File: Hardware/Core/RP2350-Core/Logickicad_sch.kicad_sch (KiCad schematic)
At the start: 31 parts, among them J1 Conn_01x10_Socket, J2 Conn_01x10_Socket, Q1 BSS123, SW1 SW_Push, U17 RP2350A, U19 W25Q16JVSNIQ, X1 12MHz

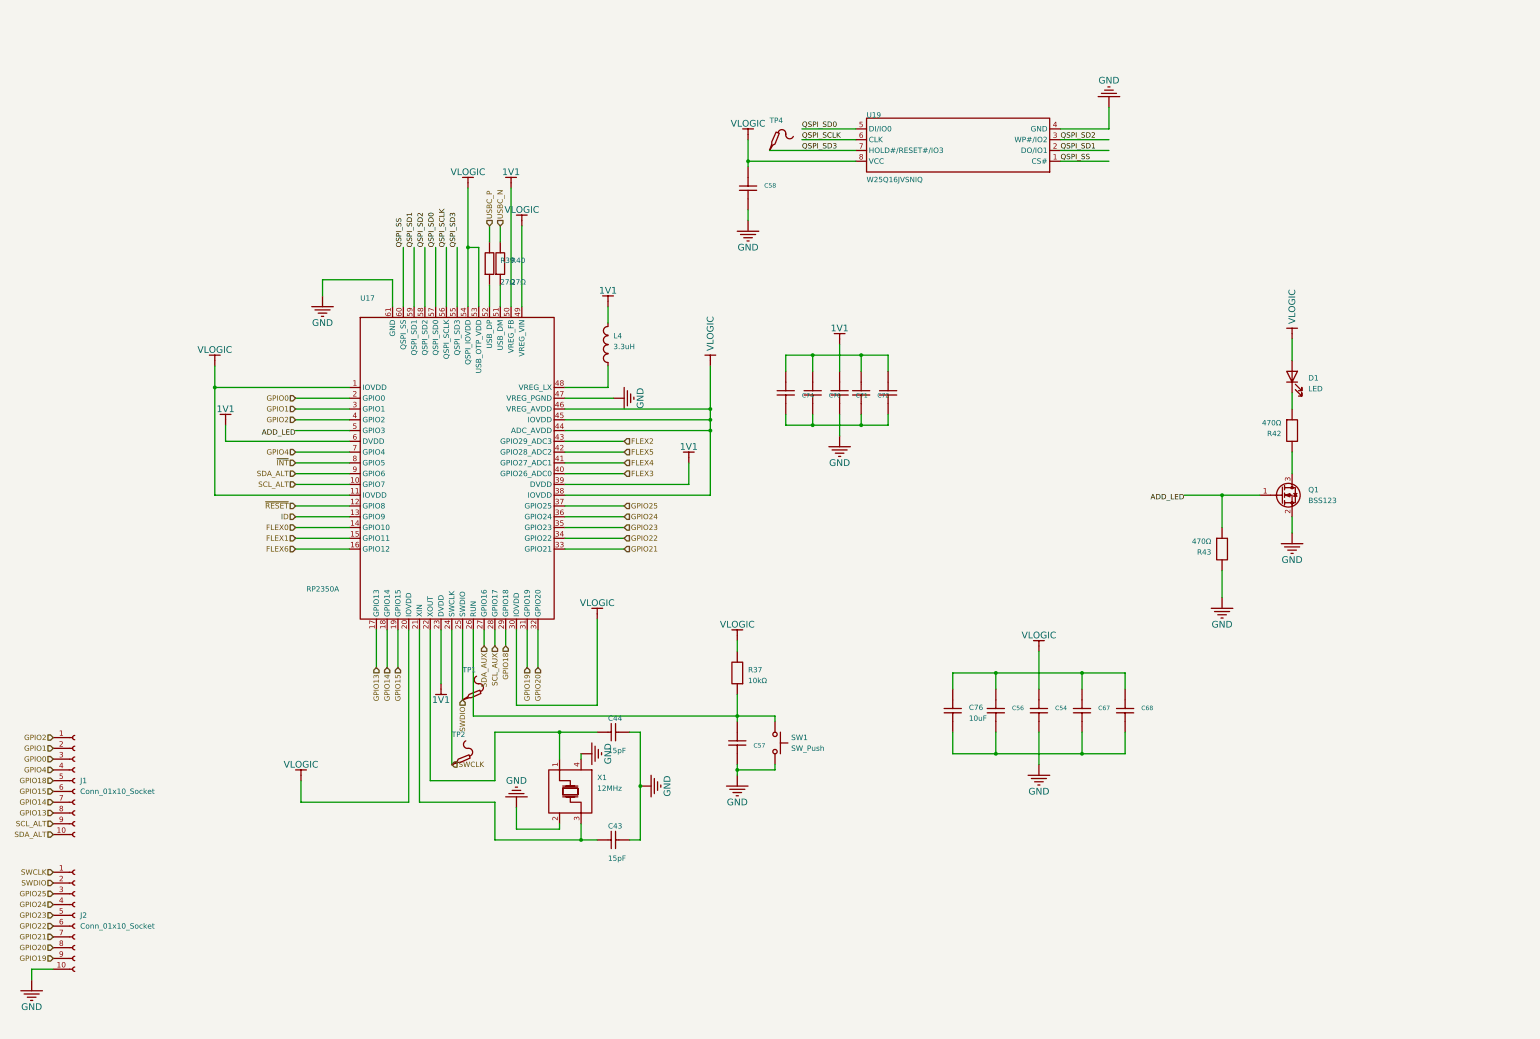
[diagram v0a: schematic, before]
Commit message: Added RP2354 with integrated flash, 80 pin and OR diode in power supply
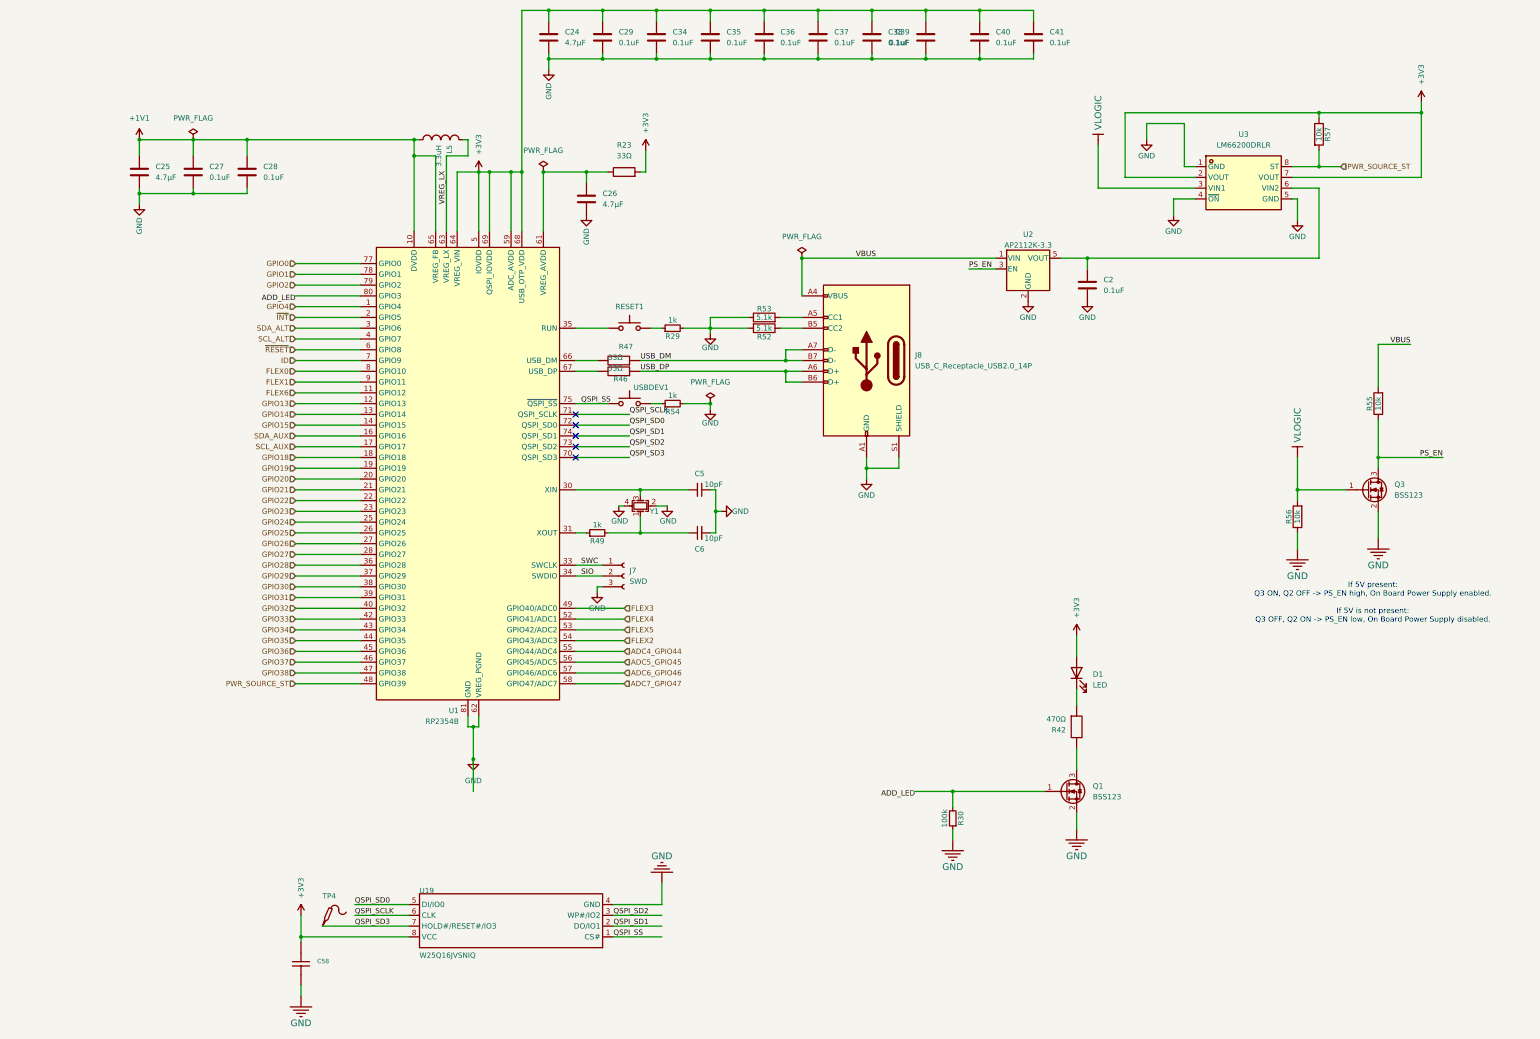
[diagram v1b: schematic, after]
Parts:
- removed C43, C44: 15pF, USBC_PD_mo-easyedapro:C0603, symbol USBC_PD_mo-easyedapro:CL10C150JB8NNNC
- removed C54, C56, C57, C67, C68, C70, C71, C72, C73, C74: 100nF, USBC_PD_mo-easyedapro:C1206, symbol USBC_PD_mo-easyedapro:1206B104K500
- removed C76: 10uF, USBC_PD_mo-easyedapro:C1206, symbol USBC_PD_mo-easyedapro:HGC1206R5106K500NSPJ
- removed J1, J2: Conn_01x10_Socket, symbol Connector:Conn_01x10_Socket
- removed L4: 3.3uH, USBC_PD_mo-easyedapro:L1210, symbol USBC_PD_mo-easyedapro:CMI322513U3R3KT
- removed R37: 10kΩ, USBC_PD_mo-easyedapro:R0805, symbol USBC_PD_mo-easyedapro:FRC0805J103TS
- removed R39, R40: 27Ω, USBC_PD_mo-easyedapro:R0805, symbol USBC_PD_mo-easyedapro:CR0805F827R0G
- removed R43: 470Ω, USBC_PD_mo-easyedapro:R0805, symbol USBC_PD_mo-easyedapro:FRC0805J103TS
- removed SW1: SW_Push, symbol Switch:SW_Push
- removed TP1, TP2: (no value), USBC_PD_mo-easyedapro:Test-Point-0.5mm, symbol USBC_PD_mo-easyedapro:Test-Point
- removed U17: RP2350A, USBC_PD_mo-easyedapro:QFN-60_L7.0-W7.0-P0.40-TL-EP3.4, symbol USBC_PD_mo-easyedapro:RP2350A_C42411118
- removed X1: 12MHz, USBC_PD_mo-easyedapro:CRYSTAL-SMD_4P-L3.2-W2.5-BL, symbol USBC_PD_mo-easyedapro:X322512MSB4SI
- added C2, C27, C28, C29, C34, C35, C36, C37, C38, C39, C40, C41: 0.1uF, Capacitor_SMD:C_0402_1005Metric, symbol Device:C
- added C24, C25, C26: 4.7μF, Capacitor_SMD:C_0402_1005Metric, symbol Device:C
- added C5, C6: 10pF, Capacitor_SMD:C_0603_1608Metric, symbol Device:C_Small
- added J7: SWD, Connector_PinHeader_2.54mm:PinHeader_1x03_P2.54mm_Vertical, symbol Connector:Conn_01x03_Socket
- added J8: USB_C_Receptacle_USB2.0_14P, USB-C-Power-tester:TYPE-C-31-M-14, symbol Connector:USB_C_Receptacle_USB2.0_14P
- added L5: 3.3uH, SpaghettiLAB:L1210, symbol USBC_PD_mo-easyedapro:CMI322513U3R3KT
- added Q3: BSS123, Package_TO_SOT_SMD:SOT-23, symbol Transistor_FET:BSS123
- added R23: 33Ω, Resistor_SMD:R_0402_1005Metric, symbol Device:R
- added R29, R49, R54: 1k, Resistor_SMD:R_0603_1608Metric, symbol wazombi:R_Small
- added R30: 100k, Resistor_SMD:R_0603_1608Metric, symbol wazombi:R_Small
- added R46, R47: 33Ω, SpaghettiLAB:R0805, symbol USBC_PD_mo-easyedapro:CR0805F827R0G
- added R52, R53: 5.1k, Resistor_SMD:R_0402_1005Metric, symbol Device:R
- added R55, R56, R57: 10k, Resistor_SMD:R_0402_1005Metric, symbol Device:R
- added RESET1, USBDEV1: SW_Push, USB-C-Power-tester:SW_Push_1P1T_NO_CK_KMR2, symbol Switch:SW_Push
- added U1: RP2354B, Package_DFN_QFN:QFN-80-1EP_10x10mm_P0.4mm_EP3.4x3.4mm, symbol MCU_RaspberryPi:RP2354B
- added U2: AP2112K-3.3, Package_TO_SOT_SMD:SOT-23-5, symbol Regulator_Linear:AP2112K-3.3
- added U3: LM66200DRLR, SpaghettiLAB:SOT-583-8_L2.1-W1.2-P0.50-LS1.6-BL, symbol SpaghettiLAB:LM66200DRLR
- added Y1: Crystal, Crystal:Crystal_SMD_3225-4Pin_3.2x2.5mm, symbol wazombi:Crystal_GND24_Small
- C58: footprint USBC_PD_mo-easyedapro:C1206 -> SpaghettiLAB:C1206
- R42: footprint USBC_PD_mo-easyedapro:R0805 -> SpaghettiLAB:R0805
- U19: footprint USBC_PD_mo-easyedapro:SOP-8_L4.9-W3.9-P1.27-LS6.0-BL -> SpaghettiLAB:SOP-8_L4.9-W3.9-P1.27-LS6.0-BL
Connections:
- net ADD_LED: now also R30.2, U1.80 (GPIO3)
- net FLEX0: now also U1.8 (GPIO10)
- net FLEX1: now also U1.9 (GPIO11)
- net FLEX2: now also U1.54 (GPIO43/ADC3)
- net FLEX3: now also U1.49 (GPIO40/ADC0)
- net FLEX4: now also U1.52 (GPIO41/ADC1)
- net FLEX5: now also U1.53 (GPIO42/ADC2)
- net FLEX6: now also U1.11 (GPIO12)
- net GND: now also C2.1, C24.2, C25.2, C26.2, C27.1, C28.1, C29.1, C34.1, C35.1, C36.1, C37.1, C38.1, C39.1, C40.1, C41.1, C5.1, C6.2, J7.3 (Pin_3), J8.A1 (GND), J8.A12 (GND), J8.B1 (GND), J8.B12 (GND), J8.S1 (SHIELD), Q3.2 (S), R29.2, R30.1, R52.2, R53.1, R54.2, R56.1, U1.62 (VREG_PGND), U1.81 (GND), U2.2 (GND), U3.1 (GND), U3.4 (~{ON}), U3.5 (GND), Y1.2, Y1.4
- net GPIO0: now also U1.77 (GPIO0)
- net GPIO1: now also U1.78 (GPIO1)
- net GPIO13: now also U1.12 (GPIO13)
- net GPIO14: now also U1.13 (GPIO14)
- net GPIO15: now also U1.14 (GPIO15)
- net GPIO18: now also U1.18 (GPIO18)
- net GPIO19: now also U1.19 (GPIO19)
- net GPIO2: now also U1.79 (GPIO2)
- net GPIO20: now also U1.20 (GPIO20)
- net GPIO21: now also U1.21 (GPIO21)
- net GPIO22: now also U1.22 (GPIO22)
- net GPIO23: now also U1.23 (GPIO23)
- net GPIO24: now also U1.25 (GPIO24)
- net GPIO25: now also U1.26 (GPIO25)
- net GPIO4: now also U1.1 (GPIO4)
- net ID: now also U1.7 (GPIO9)
- net QSPI_SCLK: now also U1.71 (QSPI_SCLK)
- net QSPI_SD0: now also U1.72 (QSPI_SD0)
- net QSPI_SD1: now also U1.74 (QSPI_SD1)
- net QSPI_SD2: now also U1.73 (QSPI_SD2)
- net QSPI_SD3: now also U1.70 (QSPI_SD3)
- net QSPI_SS: now also U1.75 (~{QSPI_SS}), USBDEV1.1
- net SCL_ALT: now also U1.4 (GPIO7)
- net SCL_AUX: now also U1.17 (GPIO17)
- net SDA_ALT: now also U1.3 (GPIO6)
- net SDA_AUX: now also U1.16 (GPIO16)
- net VLOGIC: now also Q3.1 (G), R56.2, U3.3 (VIN1); no longer C58.2, D1.2 (A), U19.8 (VCC)
- net ~{INT}: now also U1.2 (GPIO5)
- net ~{RESET}: now also U1.6 (GPIO8)
- new net: C2.2, U2.5 (VOUT), U3.6 (VIN2)
- new net: C5.2, U1.30 (XIN), Y1.3
- new net: R54.1, USBDEV1.2
- new net: R46.2, U1.67 (USB_DP)
- new net: C26.1, R23.1, U1.61 (VREG_AVDD)
- new net: J8.A5 (CC1), R53.2
- new net: J8.B5 (CC2), R52.1
- new net: R49.1, U1.31 (XOUT)
- new net: C6.1, R49.2, Y1.1
- new net: R47.2, U1.66 (USB_DM)
- new net: RESET1.1, U1.35 (RUN)
- new net: R29.1, RESET1.2
- new net +1V1: C25.1, C27.2, C28.2, L5.1, U1.10 (DVDD), U1.32 (DVDD), U1.51 (DVDD), U1.65 (VREG_FB)
- new net +3V3: C24.1, C29.2, C34.2, C35.2, C36.2, C37.2, C38.2, C39.2, C40.2, C41.2, C58.2, D1.2 (A), R23.2, R57.1, U1.15 (IOVDD), U1.24 (IOVDD), U1.29 (IOVDD), U1.41 (IOVDD), U1.5 (IOVDD), U1.50 (IOVDD), U1.59 (ADC_AVDD), U1.60 (IOVDD), U1.64 (VREG_VIN), U1.68 (USB_OTP_VDD), U1.69 (QSPI_IOVDD), U1.76 (IOVDD), U19.8 (VCC), U3.2 (VOUT), U3.7 (VOUT)
- new net ADC4_GPIO44: U1.55 (GPIO44/ADC4)
- new net ADC5_GPIO45: U1.56 (GPIO45/ADC5)
- new net ADC6_GPIO46: U1.57 (GPIO46/ADC6)
- new net ADC7_GPIO47: U1.58 (GPIO47/ADC7)
- new net GPIO26: U1.27 (GPIO26)
- new net GPIO27: U1.28 (GPIO27)
- new net GPIO28: U1.36 (GPIO28)
- new net GPIO29: U1.37 (GPIO29)
- new net GPIO30: U1.38 (GPIO30)
- new net GPIO31: U1.39 (GPIO31)
- new net GPIO32: U1.40 (GPIO32)
- new net GPIO33: U1.42 (GPIO33)
- new net GPIO34: U1.43 (GPIO34)
- new net GPIO35: U1.44 (GPIO35)
- new net GPIO36: U1.45 (GPIO36)
- new net GPIO37: U1.46 (GPIO37)
- new net GPIO38: U1.47 (GPIO38)
- new net PS_EN: Q3.3 (D), R55.1, U2.3 (EN)
- new net PWR_SOURCE_ST: R57.2, U1.48 (GPIO39), U3.8 (ST)
- new net SIO: J7.2 (Pin_2), U1.34 (SWDIO)
- new net SWC: J7.1 (Pin_1), U1.33 (SWCLK)
- new net USB_DM: J8.A7 (D-), J8.B7 (D-), R47.1
- new net USB_DP: J8.A6 (D+), J8.B6 (D+), R46.1
- new net VBUS: J8.A4 (VBUS), J8.A9 (VBUS), J8.B4 (VBUS), J8.B9 (VBUS), R55.2, U2.1 (VIN)
- new net VREG_LX: L5.2, U1.63 (VREG_LX)
- no-connect marks 0 -> 5
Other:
- note added: "If 5V present: Q3 ON, Q2 OFF -> PS_EN high, On Board Power Supply enabled. If 5V is not present: Q3 OFF, Q2 ON -> PS_EN low, On Board Power Supply disabled."
- moved on the sheet: D1, Q1, R42
